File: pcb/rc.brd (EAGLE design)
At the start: 64.8 x 69.2 mm, 79 parts, among them IC2 TP4056

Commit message: pcb
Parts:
- removed FLASH1, FLASH2, GND, RX, SERVO_CONTROL, SERVO_GND, SERVO_POWER, TX: WIREPADSMD5-1,8, wirepad:5-1,8
- removed JP2, JP3: (no value), pinhead:1X03
- added JP4, JP5: (no value), my:1X03
- JP1: device pinhead:1X03 -> my:1X03
- JP6: device pinhead:1X02 -> my:1X02
- moved R27 48.7 mm to (53.3, 19.7)
- moved MOTOR_A 20.6 mm to (26.0, 5.71)
- moved MOTOR_B 19.7 mm to (21.3, 5.71)
- moved JP1 8.64 mm to (14.3, 6.67), turned to 0 degrees
- moved R22 5.40 mm to (24.8, 6.67), turned to 90 degrees
- moved JP6 4.02 mm to (5.71, 6.67), turned to 0 degrees
- moved R14 3.70 mm to (22.2, 16.8)
- moved IC1 3.19 mm to (14.9, 11.7)
- moved R6 3.19 mm to (17.8, 13.0)
- moved T11 3.19 mm to (20.3, 12.4)
- moved BAT- 0.95 mm to (35.9, 5.71)
- moved R13 0.90 mm to (26.0, 11.4), turned to 180 degrees
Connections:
- net SERVO_CONTROL renamed SERVO#1_CTRL
- removed net N$29: R22.1, SERVO_CONTROL.1
- new net SERVO#2_CTRL: JP1.1, R18.1, U1.GPIO2
- net 5V: now also JP1.2
- net GND: now also JP1.3, JP4.3, JP5.3, JP6.2; no longer FLASH2.1, GND.1, SERVO_GND.1
- net N$21: now also JP6.1; no longer FLASH1.1
- net N$22: now also JP4.1, R22.1; no longer R18.1, U1.GPIO2
- net N$30: now also JP4.2; no longer SERVO_POWER.1
- net RX: now also JP5.2; no longer RX.1
- net TX: now also JP5.1; no longer TX.1
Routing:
- net SERVO#2_CTRL: track 0.00 -> 31.8 mm, vias 0 -> 2
- net N$29: track 13.4 -> 0.00 mm
- net N$21: track 19.3 -> 28.1 mm, vias 1 -> 2
- net N$4: track 23.4 -> 16.3 mm
- net BAT_PROT: track 62.3 -> 56.9 mm
- net SERVO#1_CTRL: track 18.9 -> 23.8 mm
- net N$22: track 4.29 -> 8.67 mm
- net TX: track 33.4 -> 37.7 mm, vias 0 -> 1
- net N$36: track 3.87 -> 0.00 mm
- net RX: track 32.1 -> 35.8 mm, vias 0 -> 1
- net BAT_CHECK: track 14.7 -> 11.8 mm
- net N$35: track 2.67 -> 0.13 mm
- net N$30: track 0.00 -> 2.54 mm
- net N$37: track 6.69 -> 5.76 mm
- net GND: track 277.1 -> 277.8 mm

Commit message: pcb
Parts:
- removed R14, R23, R26, R27: 0, skydrop:R1206
- moved LED1 27.7 mm to (27.3, 22.2)
- moved R21 27.1 mm to (27.9, 25.1)
- moved R29 24.6 mm to (26.7, 37.8)
- moved R22 22.0 mm to (3.17, 10.8), turned to 0 degrees
- moved MOTOR_A 21.3 mm to (4.76, 5.71)
- moved MOTOR_B 21.0 mm to (0.32, 5.71)
- moved T11 15.4 mm to (22.5, 27.6), turned to 180 degrees
- moved IC1 13.7 mm to (22.5, 23.2), turned to 180 degrees
- moved R6 12.6 mm to (20.0, 25.4)
- moved JP1 8.31 mm to (22.5, 7.62)
- moved JP4 8.31 mm to (22.5, 5.08)
- moved JP6 8.31 mm to (14.0, 7.62)
- moved JP5 8.31 mm to (12.7, 5.08)
- moved C6 6.70 mm to (21.3, 14.0)
- moved IC3 5.41 mm to (16.5, 14.6)
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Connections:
- removed net N$14 (its old number): R14.1, T11.1
- removed net N$24: C6.1, IC3.1, IC3.3, R29.1
- removed net N$30: JP4.2, R23.1
- removed net N$33: R26.1, T1.1, T3.1
- removed net N$35: R26.2, R27.1
- new net N$29: C7.2, C8.+, D5.C, IC4.2, R29.2
- net 5V: now also C6.1, IC3.1, IC3.3, JP4.2, R29.1; no longer C7.2, C8.+, D5.C, IC4.2, R23.2, R29.2
- net BAT_CHECK: now also T11.1; no longer R14.2
- net N$36: now also T1.1, T3.1; no longer R27.2
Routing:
- net N$29: track 0.00 -> 23.0 mm
- net N$36: track 0.00 -> 20.6 mm
- net GND: track 277.8 -> 293.3 mm, vias 2 -> 3
- net 5V: track 55.0 -> 44.5 mm, vias 0 -> 1
- net N$22: track 8.67 -> 19.0 mm
- net N$24: track 8.23 -> 0.00 mm
- net N$21: track 28.1 -> 35.7 mm
- net RX: track 35.8 -> 42.3 mm
- net SERVO#2_CTRL: track 31.8 -> 37.6 mm
- net TX: track 37.7 -> 43.3 mm
- net N$2: track 5.99 -> 10.4 mm
- net BAT_CHRG: track 21.2 -> 25.5 mm
- net N$33: track 3.81 -> 0.00 mm
- net VCC: track 76.1 -> 72.4 mm
- net N$27: track 0.00 -> 3.53 mm
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
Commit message: pcb
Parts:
- removed D5: (no value), adafruit:SMADIODE
- added D1: (no value), semicon-smd-ipc:SMB
- C5, C6: device skydrop:C1206 -> skydrop:C0805
- C8, C9: device adafruit:D/7343-31W -> adafruit:CT6032
- L1: value (none) -> DR74; device inductor-neosid:MS85 -> inductors:DR74
- R2: device skydrop:R0805 -> my:R0805
- moved R5 1.62 mm to (7.30, 32.4)
- moved T12 0.71 mm to (29.8, 32.1)
- moved C7 0.71 mm to (28.6, 23.2)
- moved IC4 0.71 mm to (29.8, 28.3)
- moved R25 0.71 mm to (32.1, 23.5)
- moved T10 0.63 mm to (10.8, 31.8), turned to 90 degrees
- moved L1 0.63 mm to (35.2, 29.5), turned to 90 degrees
- moved C6 0.45 mm to (21.0, 14.3)
- moved R6 0.32 mm to (19.7, 25.4)
- moved BAT+ 0.32 mm to (31.1, 5.40)
- moved BAT- 0.32 mm to (35.6, 5.40)
- moved MOTOR_A 0.32 mm to (4.76, 5.40)
- moved MOTOR_B 0.32 mm to (0.32, 5.40)
- moved C9 0.32 mm to (31.4, 19.1)
- moved IC1 0.32 mm to (22.2, 23.2)
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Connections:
- net N$29: now also D1.1; no longer D5.C
- net N$3: now also D1.2; no longer D5.A
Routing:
- net GND: track 293.3 -> 286.1 mm
- net SERVO#2_CTRL: track 37.6 -> 35.1 mm, vias 2 -> 1
- net N$4: track 19.7 -> 17.8 mm
- net H_PWM: track 4.58 -> 5.85 mm
- net N$31: track 6.51 -> 5.29 mm
- net N$29: track 23.0 -> 24.1 mm
- net BAT_PROT: track 54.5 -> 55.6 mm
- net N$3: track 9.28 -> 10.3 mm
- net N$36: track 20.6 -> 19.6 mm
- net 5V: track 44.5 -> 43.7 mm, vias 1 -> 2
- net N$22: track 19.0 -> 18.2 mm, vias 1 -> 0
- net N$18: track 2.93 -> 3.57 mm
- net N$8: track 9.26 -> 8.70 mm
- net N$21: track 35.7 -> 35.2 mm, vias 2 -> 1
- net RX: track 42.3 -> 42.4 mm, vias 1 -> 0
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
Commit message: pcb
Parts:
- moved MOTOR_A 0.95 mm to (5.71, 5.40)
- moved R22 0.71 mm to (3.81, 10.5)
- moved MOTOR_B 0.64 mm to (0.95, 5.40)
- moved R19 0.32 mm to (4.76, 21.9)
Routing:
- net SERVO#2_CTRL: track 35.1 -> 34.3 mm
- net N$22: track 18.2 -> 17.5 mm
- net N$21: track 35.2 -> 34.5 mm

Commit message: pcb
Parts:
- removed R22: 0, skydrop:R1206
- added LED2: (no value), led:CHIPLED_0805
- moved R17 5.72 mm to (1.27, 33.0)
- moved R13 5.12 mm to (33.0, 13.7), flipped to the bottom, turned to 270 degrees
- moved IC1 1.31 mm to (21.9, 24.4)
- moved R24 1.31 mm to (34.3, 37.5)
- moved R29 1.31 mm to (26.4, 39.1)
- moved T10 1.31 mm to (10.5, 33.0)
- moved C7 1.31 mm to (28.3, 24.4)
- moved D2 1.31 mm to (13.3, 24.4)
- moved J1 1.31 mm to (31.4, 42.5)
- moved R15 1.31 mm to (20.6, 36.2)
- moved R16 1.31 mm to (20.6, 32.1)
- moved R2 1.31 mm to (8.26, 24.4)
- moved R3 1.31 mm to (17.1, 33.0)
- moved R4 1.31 mm to (14.0, 33.0)
- moved R5 1.31 mm to (6.99, 33.7)
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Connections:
- removed net N$22: JP4.1, R22.1
- new net N$24: LED2.A, R17.1
- net H_PWM: now also R18.1, U1.GPIO2; no longer U1.GPIO5
- net N$21: now also LED2.C; no longer R17.1
- net SERVO#1_CTRL: now also JP1.1; no longer R22.2
- net SERVO#2_CTRL: now also JP4.1, U1.GPIO5; no longer JP1.1, R18.1, U1.GPIO2
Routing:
- net SERVO#1_CTRL: track 23.1 -> 40.9 mm
- net N$22: track 17.5 -> 0.00 mm
- net SERVO#2_CTRL: track 34.3 -> 46.0 mm, vias 1 -> 0
- net H_PWM: track 5.85 -> 12.7 mm
- net GND: track 285.8 -> 282.2 mm, vias 3 -> 2
- net V_CHRG: track 40.7 -> 37.6 mm
- net N$24: track 0.00 -> 2.28 mm
- net N$21: track 34.5 -> 35.5 mm, vias 1 -> 3
- net BAT_CHRG: track 25.5 -> 26.1 mm
- net N$36: track 19.2 -> 18.7 mm
- net N$9: track 17.3 -> 16.7 mm
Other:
- board size 64.8 x 69.2 mm -> 41 x 41.6 mm

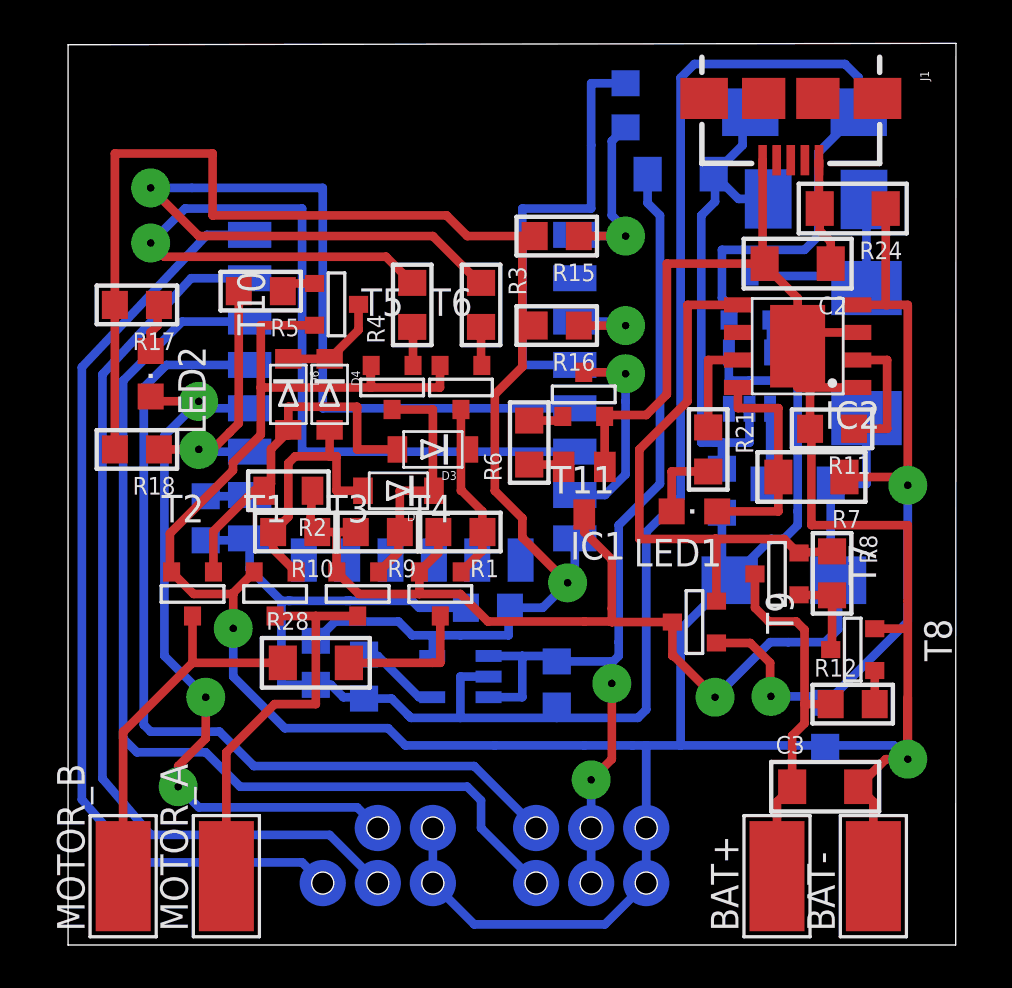
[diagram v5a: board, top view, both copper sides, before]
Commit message: pcb 0.5mm
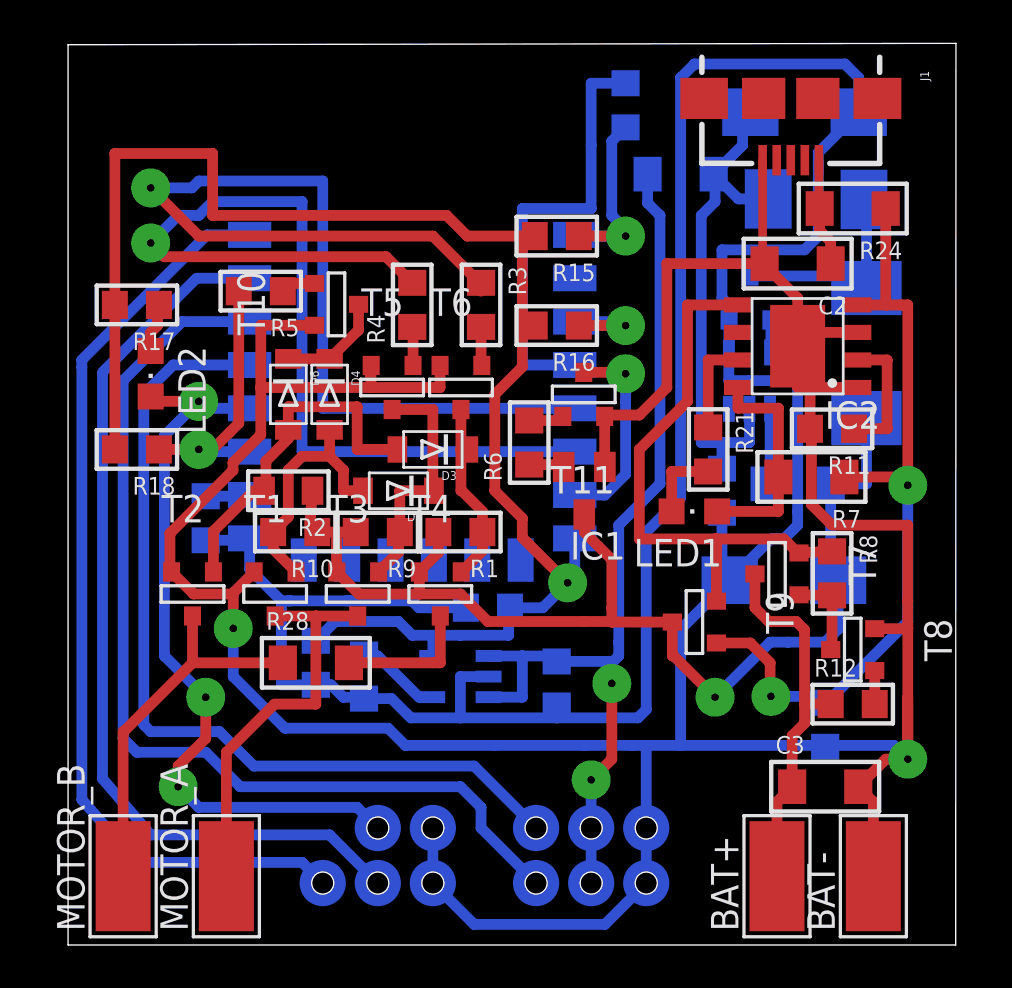
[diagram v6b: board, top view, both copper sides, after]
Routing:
- net GND: track 282.2 -> 281.5 mm
- net N$6: track 12.5 -> 11.9 mm

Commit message: add values for some components
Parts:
- C1: value (none) -> 0.1uF
- C2, C3: value (none) -> 10uF
- C4: value (none) -> 0.01uF
- C5, C6: value (none) -> 1uF
- D1: value (none) -> SS26
- IC1: value (none) -> STM809S
- IC3: value (none) -> 3.3v 300mA low-drop
- IC4: value (none) -> NCP1450
- R1, R10, R12, R2, R5, R9: value (none) -> 100k
- R11: value (none) -> 1.2k
- R13, R15, R16, R18, R19, R3, R4, R6, R8: value (none) -> 10k
- R17, R21: value (none) -> 1k
- R24: value 0 -> 0.4
